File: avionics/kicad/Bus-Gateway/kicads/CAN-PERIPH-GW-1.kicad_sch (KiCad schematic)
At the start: 83 parts, among them U1_1 TI MSPM0G3518-Q1, U1_2 TI MSPM0G3518-Q1, U1_3 TI MSPM0G3518-Q1, U1_4 TI MSPM0G3518-Q1, U2_1 Infineon SLB 9672AU2.0, U2_2 Infineon SLB 9672AU2.0, U2_3 Infineon SLB 9672AU2.0, U2_4 Infineon SLB 9672AU2.0, U3_1 TI ISOW1044BDFMR, U3_2 TI ISOW1044BDFMR, U3_3 TI ISOW1044BDFMR, U3_4 TI ISOW1044BDFMR, U4_1 TI ISOW1412, U4_2 TI ISOW1412, U4_3 TI ISOW1412, U4_4 TI ISOW1412

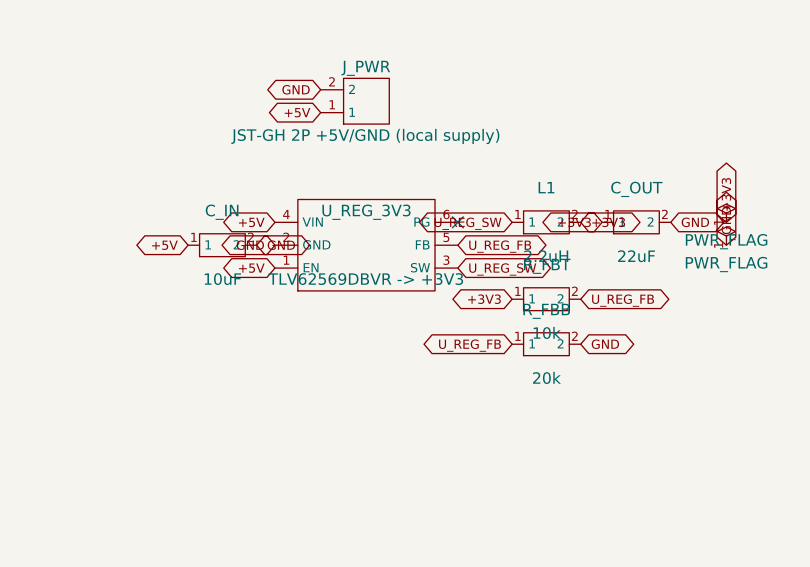
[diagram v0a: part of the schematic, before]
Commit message: fix(avionics): TLV62569 -> TLV62569PDRLR and TLV75725 -> TLV75725PDRVR package swaps; regulator circuit fixes; stale-component cleanup
Owner-approved swaps (2026-09-26, avionics/WBS.md U7.1e) using the
datasheet-verified SecureControllers library via ${SECURE_CONTROLLERS_LIB}:
- CAN-PERIPH-GW-1 U_REG_3V3, Observer U_REG_3V3/U_REG_1V2, Flight
  Engineer U_REG_3V3_H -> TLV62569PDRLR (SOT-563, 1.6 x 1.6 mm).
  Pins remapped by name; the old symbols had FB/PG swapped (gateway,
  Observer) or sat on a 3-pad SOT-23 (Flight Engineer).
- Observer U_REG_2V5 -> TLV75725PDRVR (WSON-6 2x2, EP to GND).
- Feedback dividers per TLV62569 Sec. 8.2.2.2 Eq. 2 (VFB 0.6 V):
  gateway 10k/20k (0.9 V!) -> 453k/100k = 3.318 V; Observer placeholders
  -> 453k/100k (3V3) and 100k/100k (1V2).
- Flight Engineer: EN was tied to its own 3V3 output and FB straight to
  +3V3 (would regulate at 0.6 V); EN -> +5V, added R_H_FBT 453k /
  R_H_FBB 100k. Parity 2 -> 0, ERC 0.
- tools/kicad_prune_stale.py: parity-driven removal of stale electrical
  footprints and only the copper they orphan; mounting holes are marked
  board_only + renumbered (Commo parity 93 -> 86, Observer 21 -> 17).
- New tools kicad_relink.py / kicad_add_part.py / kicad_set_value.py;
  SecureControllers entries added to every board's lib tables.

Sources: TI TLV62569 (SLVSDG1C) Pin Functions, Sec. 8.2.2.2; TI TLV757P
Fig. 4-3, Pin Functions, DRV0006A.

AI-authored: Claude Opus 5.5 (Anthropic).

Co-Authored-By: Claude Opus 5.5 <noreply@anthropic.com>
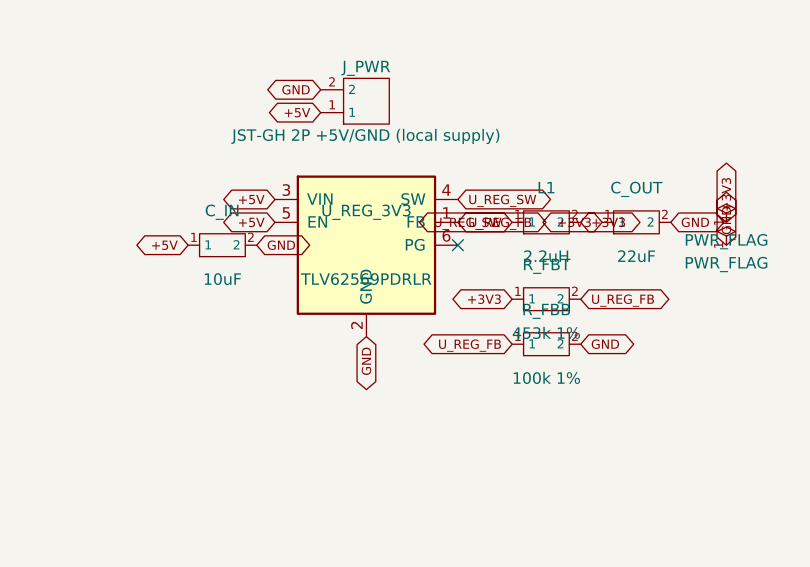
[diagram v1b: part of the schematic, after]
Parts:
- R_FBB: value 20k -> 100k 1%
- R_FBT: value 10k -> 453k 1%
- U_REG_3V3: value TLV62569DBVR -> +3V3 -> TLV62569PDRLR; footprint Package_TO_SOT_SMD:SOT-23-6 -> Package_TO_SOT_SMD:SOT-563; symbol TLV62569_DBV -> SecureControllers:TLV62569PDRL
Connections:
- net +5V: now also U_REG_3V3.3 (VIN), U_REG_3V3.5 (EN); no longer U_REG_3V3.1 (EN), U_REG_3V3.4 (VIN)
- net U_REG_FB: now also U_REG_3V3.1 (FB); no longer U_REG_3V3.5 (FB)
- net U_REG_SW: now also U_REG_3V3.4 (SW); no longer U_REG_3V3.3 (SW)
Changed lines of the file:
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@@
     (property "Intersheet References" "${INTERSHEET_REFS}" (at 25.00 15.00 0)
       (effects (font (size 1.016 1.016)) (hide yes))))
-  (symbol (lib_id "TLV62569_DBV") (at 25.00 48.00 0)
+  (symbol (lib_id "SecureControllers:TLV62569PDRL") (at 25.00 48.00 0)
     (unit 1) (exclude_from_sim no) (in_bom yes) (on_board yes) (dnp no)
     (property "Reference" "U_REG_3V3" (at 25.00 44.19 0)
       (effects (font (size 1.27 1.27))))
-    (property "Value" "TLV62569DBVR -> +3V3" (at 25.00 51.81 0)
+    (property "Value" "TLV62569PDRLR" (at 25.00 51.81 0)
       (effects (font (size 1.27 1.27))))
-    (property "Footprint" "Package_TO_SOT_SMD:SOT-23-6" (at 0 0 0)
+    (property "Footprint" "Package_TO_SOT_SMD:SOT-563" (at 0 0 0)
       (effects (font (size 1.27 1.27)) (hide yes)))
     (property "Datasheet" "https://www.ti.com/lit/ds/symlink/tlv62569.pdf" (at 0 0 0)
       (effects (font (size 1.27 1.27)) (hide yes)))
   )
-  (global_label "+5V" (shape bidirectional) (at 14.84 50.54 180)
+  (global_label "+5V" (shape bidirectional) (at 14.8400 45.4600 180)
     (effects (font (size 1.016 1.016)))
     (property "Intersheet References" "${INTERSHEET_REFS}" (at 14.84 50.54 0)
       (effects (font (size 1.016 1.016)) (hide yes))))
-  (global_label "GND" (shape bidirectional) (at 14.84 48.00 180)
+  (global_label "GND" (shape bidirectional) (at 25.0000 58.1600 270)
     (effects (font (size 1.016 1.016)))
     (property "Intersheet References" "${INTERSHEET_REFS}" (at 14.84 48.00 0)
       (effects (font (size 1.016 1.016)) (hide yes))))
-  (global_label "+5V" (shape bidirectional) (at 14.84 45.46 180)
+  (global_label "+5V" (shape bidirectional) (at 14.8400 42.9200 180)
     (effects (font (size 1.016 1.016)))
     (property "Intersheet References" "${INTERSHEET_REFS}" (at 14.84 45.46 0)
       (effects (font (size 1.016 1.016)) (hide yes))))
-  (global_label "U_REG_SW" (shape bidirectional) (at 35.16 50.54 0)
+  (global_label "U_REG_SW" (shape bidirectional) (at 35.1600 42.9200 0)
     (effects (font (size 1.016 1.016)))
     (property "Intersheet References" "${INTERSHEET_REFS}" (at 35.16 50.54 0)
       (effects (font (size 1.016 1.016)) (hide yes))))
-  (global_label "U_REG_FB" (shape bidirectional) (at 35.16 48.00 0)
+  (global_label "U_REG_FB" (shape bidirectional) (at 35.1600 45.4600 0)
     (effects (font (size 1.016 1.016)))
     (property "Intersheet References" "${INTERSHEET_REFS}" (at 35.16 48.00 0)
       (effects (font (size 1.016 1.016)) (hide yes))))
-  (no_connect (at 35.16 45.46))
+  (no_connect (at 35.1600 48.0000))
   (symbol (lib_id "L_Generic") (at 45.00 45.46 0)
     (unit 1) (exclude_from_sim no) (in_bom yes) (on_board yes) (dnp no)
@@
     (property "Reference" "R_FBT" (at 45.00 50.19 0)
       (effects (font (size 1.27 1.27))))
-    (property "Value" "10k" (at 45.00 57.81 0)
+    (property "Value" "453k 1%" (at 45.00 57.81 0)
       (effects (font (size 1.27 1.27))))
     (property "Footprint" "Resistor_SMD:R_0402_1005Metric" (at 0 0 0)
@@
     (property "Reference" "R_FBB" (at 45.00 55.19 0)
       (effects (font (size 1.27 1.27))))
-    (property "Value" "20k" (at 45.00 62.81 0)
+    (property "Value" "100k 1%" (at 45.00 62.81 0)
       (effects (font (size 1.27 1.27))))
     (property "Footprint" "Resistor_SMD:R_0402_1005Metric" (at 0 0 0)
